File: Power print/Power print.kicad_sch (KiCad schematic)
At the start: 17 parts, among them J1 USB_C_Receptacle_USB2.0_14P, U1 CH224K

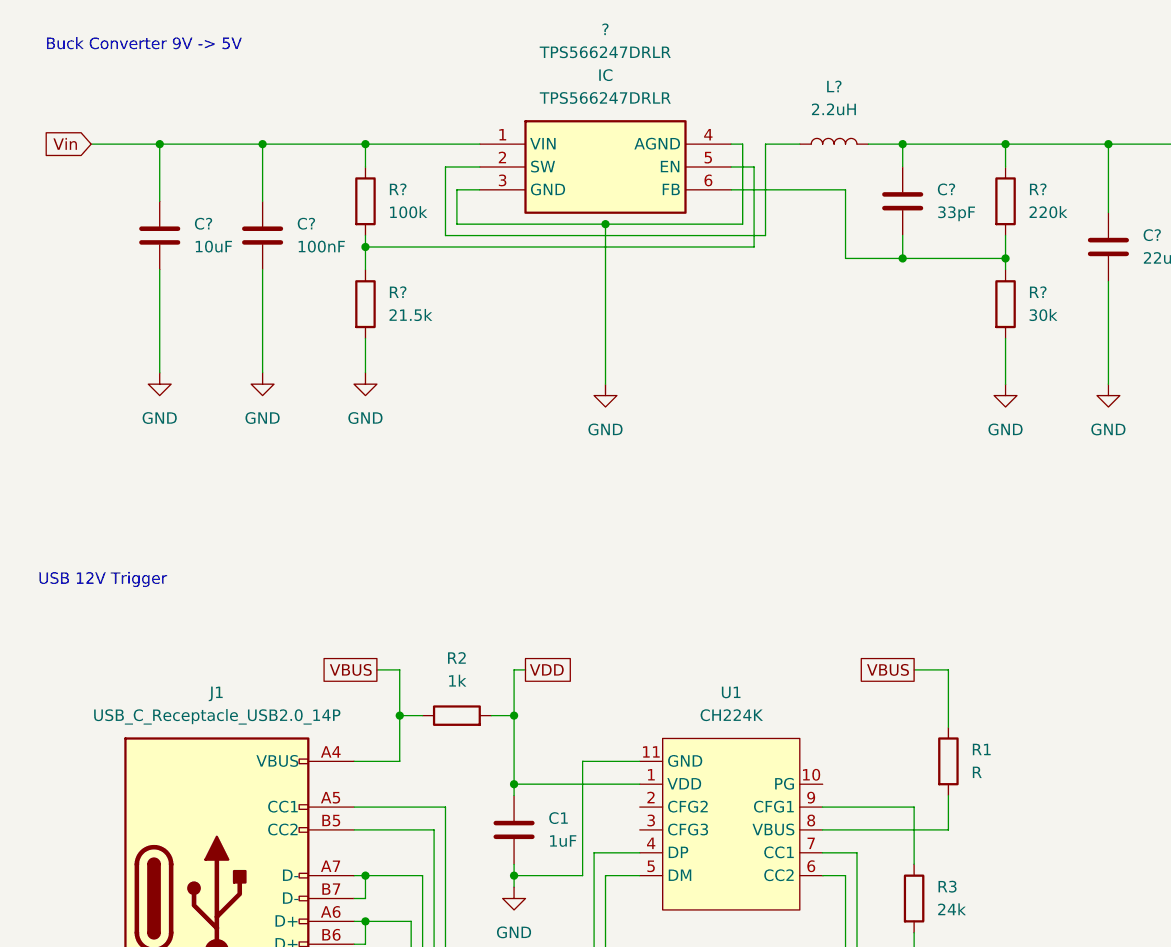
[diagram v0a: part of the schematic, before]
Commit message: Power print resistor added
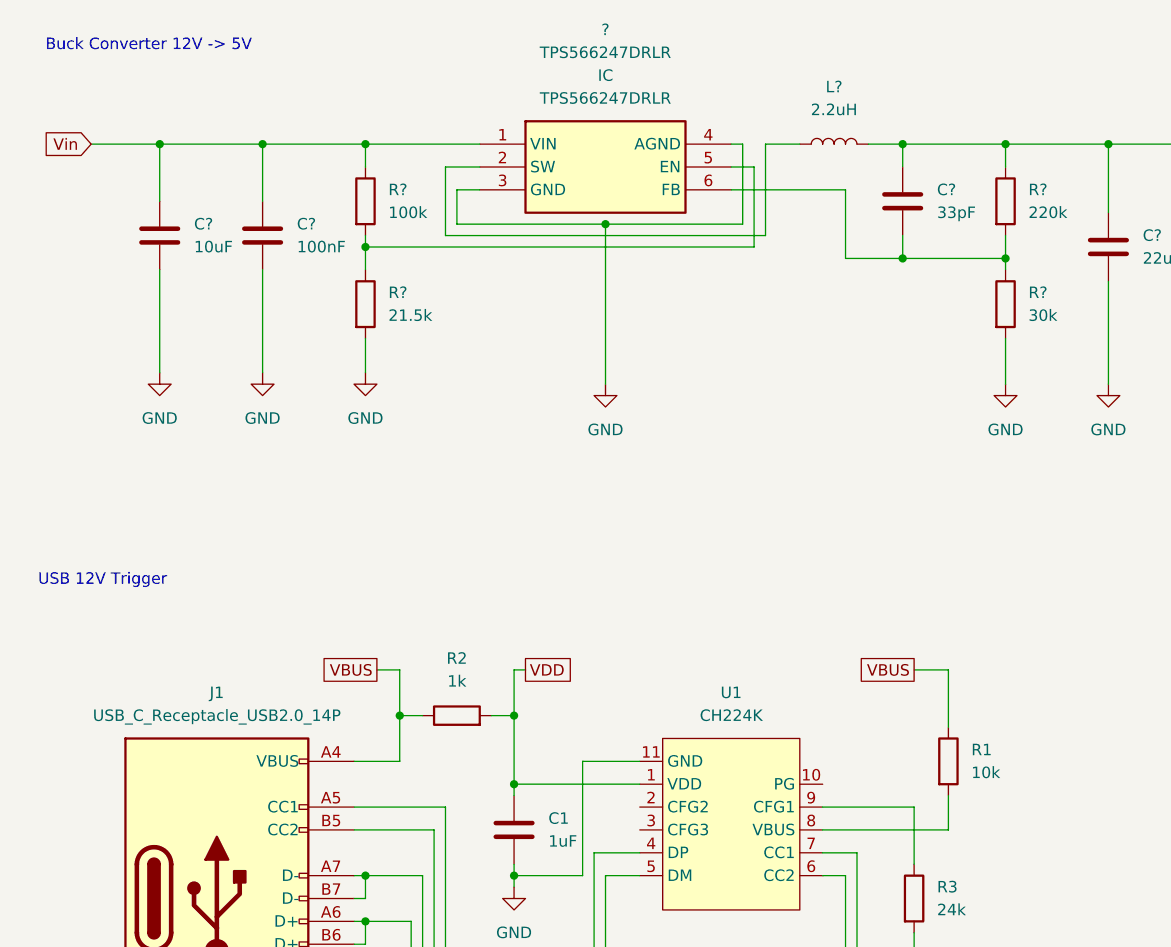
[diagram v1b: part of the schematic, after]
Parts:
- R1: value R -> 10k
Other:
- note added: "Buck Converter 12V -> 5V"
- note removed: "Buck Converter 9V -> 5V"
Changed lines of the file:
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@@
 		)
 	)
-	(text "Buck Converter 9V -> 5V"
+	(text "Buck Converter 12V -> 5V"
 		(exclude_from_sim no)
 		(at 20.32 19.05 0)
@@
 			)
 		)
-		(property "Value" "R"
+		(property "Value" "10k"
 			(at 123.19 99.0599 0)
 			(effects

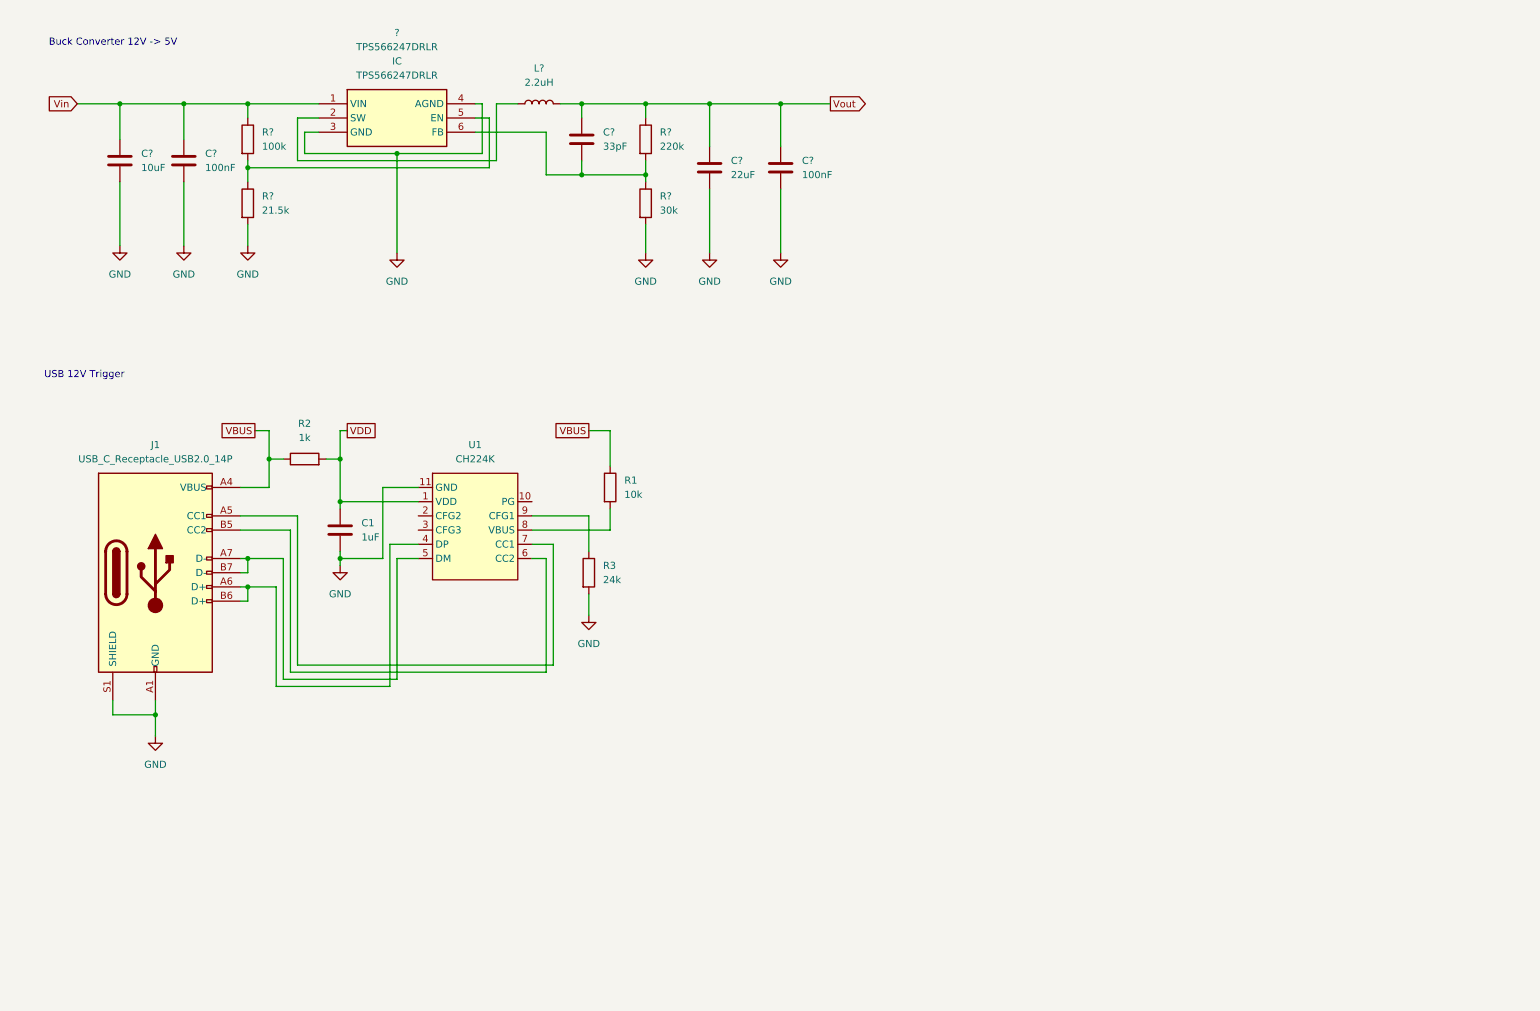
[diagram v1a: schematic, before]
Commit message: Schematics power mgmnt Pi
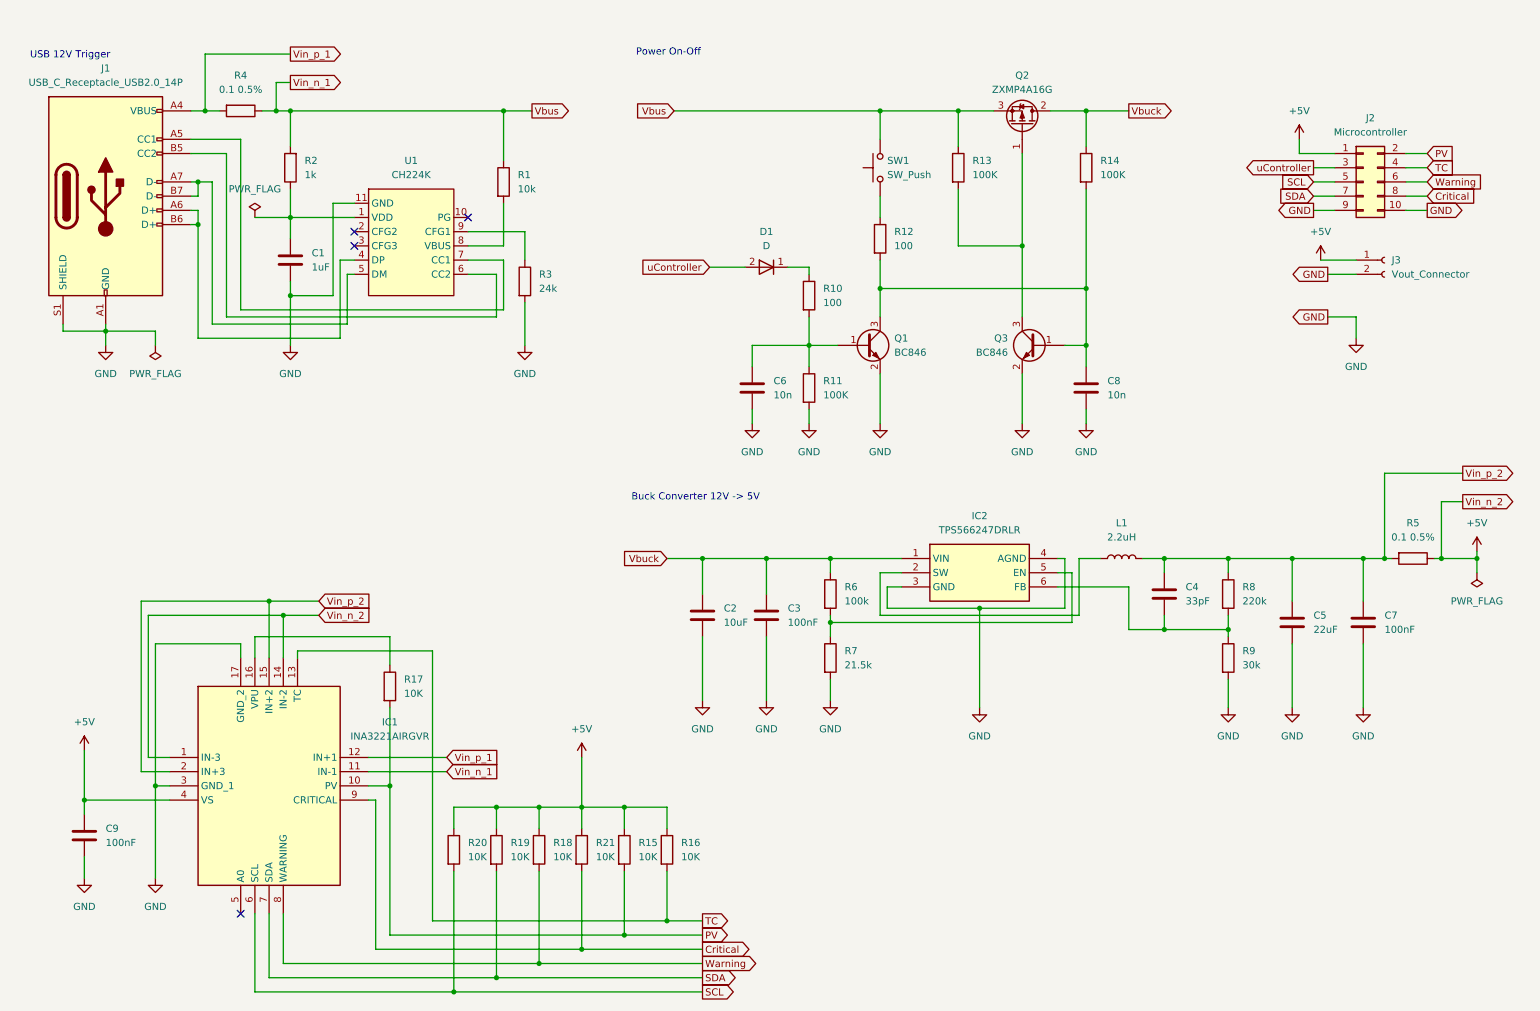
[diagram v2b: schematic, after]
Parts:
- removed ?: TPS566247DRLR, symbol Regulator_Controller:TPS566247DRLR
- added C6, C8: 10n, symbol Device:C
- added C9: 100nF, symbol Device:C
- added D1: D, symbol Simulation_SPICE:D
- added IC1: INA3221AIRGVR, QFN65P400X400X100-17N-D, symbol INA3221AIRGVR:INA3221AIRGVR
- added IC2: TPS566247DRLR, SOTFL50P160X60-6N, symbol TPS566247DRLR:TPS566247DRLR
- added J2: Microcontroller, symbol Connector_Generic:Conn_02x05_Odd_Even
- added J3: Vout_Connector, symbol Connector:Conn_01x02_Socket
- added Q1, Q3: BC846, Package_TO_SOT_SMD:SOT-23, symbol Transistor_BJT:BC846
- added Q2: ZXMP4A16G, Package_TO_SOT_SMD:SOT-223-3_TabPin2, symbol Transistor_FET:ZXMP4A16G
- added R10, R12: 100, symbol Device:R
- added R11, R13, R14: 100K, symbol Device:R
- added R15, R16, R17, R18, R19, R20, R21: 10K, symbol Device:R
- added R4, R5: 0.1 0.5%, Resistor_SMD:R_2512_6332Metric, symbol Device:R
- added SW1: SW_Push, Connector_PinHeader_1.27mm:PinHeader_1x02_P1.27mm_Vertical, symbol Switch:SW_Push
- R2: footprint (none) -> Resistor_SMD:R_0805_2012Metric
- gave numbers to parts that had none: 10
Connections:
- net GND: now also C6.2, C8.2, C9.2, IC1.17 (GND_2), IC1.3 (GND_1), IC2.3 (GND), IC2.4 (AGND), J2.10 (Pin_10), J2.9 (Pin_9), J3.2 (Pin_2), Q1.2 (E), Q3.2 (E), R11.2
- net at L1.1: now also IC2.2 (SW)
- net at R6.2, R7.1: now also IC2.5 (EN)
- net at C4.2, R8.2, R9.1: now also IC2.6 (FB)
- net VBUS renamed Vin_p_1
- net Vin_p_1: now also IC1.12 (IN+1), R4.2; no longer R1.1, R2.1
- net VDD: no longer names the net of C1.1, U1.1 (VDD)
- net VDD: now also R2.1; no longer R2.2
- net Vin renamed Vbuck
- net Vbuck: now also IC2.1 (VIN), Q2.2 (D), R14.1
- net Vout renamed Vin_p_2
- net Vin_p_2: now also IC1.15 (IN+2), IC1.2 (IN+3), R5.2
- new net: R12.1, SW1.1
- new net: C8.1, Q1.3 (C), Q3.1 (B), R12.2, R14.2
- new net: D1.1 (K), R10.1
- new net: C6.1, Q1.1 (B), R10.2, R11.1
- new net: IC1.16 (VPU), R17.1
- new net: Q2.1 (G), Q3.3 (C), R13.2
- new net +5V: C9.1, IC1.1 (IN-3), IC1.14 (IN-2), IC1.4 (VS), J2.1 (Pin_1), J3.1 (Pin_1), R15.1, R16.1, R18.1, R19.1, R20.1, R21.1, R5.1
- new net Critical: IC1.9 (CRITICAL), J2.8 (Pin_8), R21.2
- new net PV: IC1.10 (PV), J2.2 (Pin_2), R15.2, R17.2
- new net SCL: IC1.6 (SCL), J2.5 (Pin_5), R20.2
- new net SDA: IC1.7 (SDA), J2.7 (Pin_7), R19.2
- new net TC: IC1.13 (TC), J2.4 (Pin_4), R16.2
- new net Vbus: IC1.11 (IN-1), Q2.3 (S), R1.1, R13.1, R2.2, R4.1, SW1.2
- new net Warning: IC1.8 (WARNING), J2.6 (Pin_6), R18.2
- new net uController: D1.2 (A), J2.3 (Pin_3)
- no-connect marks 0 -> 4
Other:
- note added: "Power On-Off"
- moved on the sheet: C1, C2, C3, C4, C5, C7, J1, L1, R1, R2, R3, R6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

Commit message: Added title for power measurement
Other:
- note added: "Power measurement"
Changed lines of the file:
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@@
+		)
+	)
+	(text "Power measurement"
+		(exclude_from_sim no)
+		(at 26.67 111.252 0)
+		(effects
+			(font
+				(size 1.27 1.27)
+			)
 		)
 	)
